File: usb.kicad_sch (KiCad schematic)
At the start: 90 parts, among them J16 USB-C_GCT_USB4105-GF-A, J4 USB-C_GCT_USB4105-GF-A

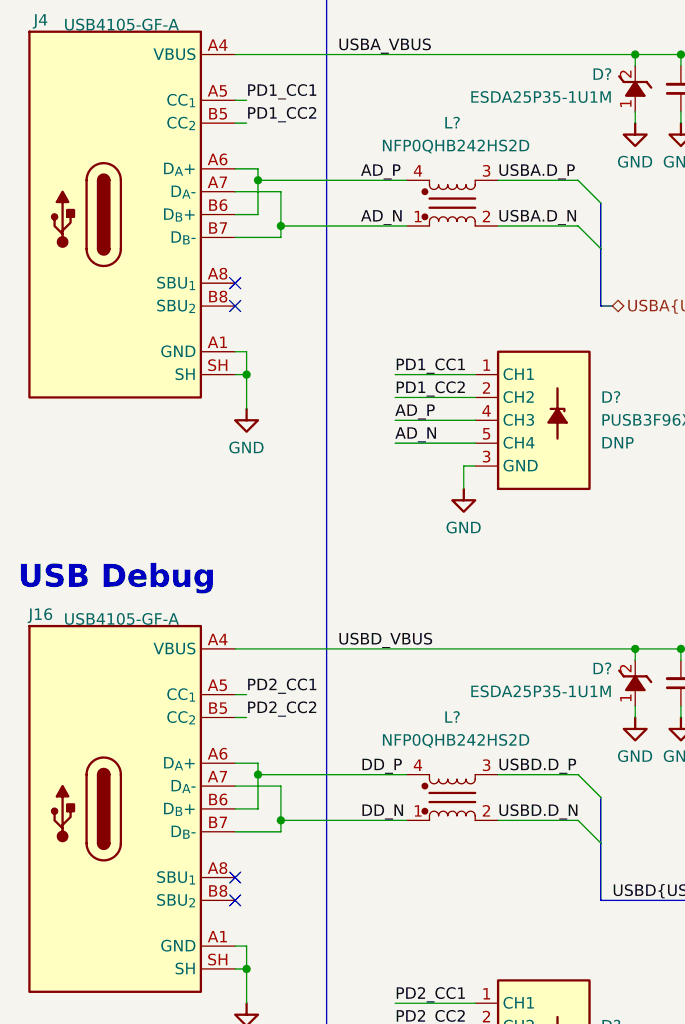
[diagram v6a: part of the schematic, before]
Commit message: [#54617] Migrate to KiCad 7
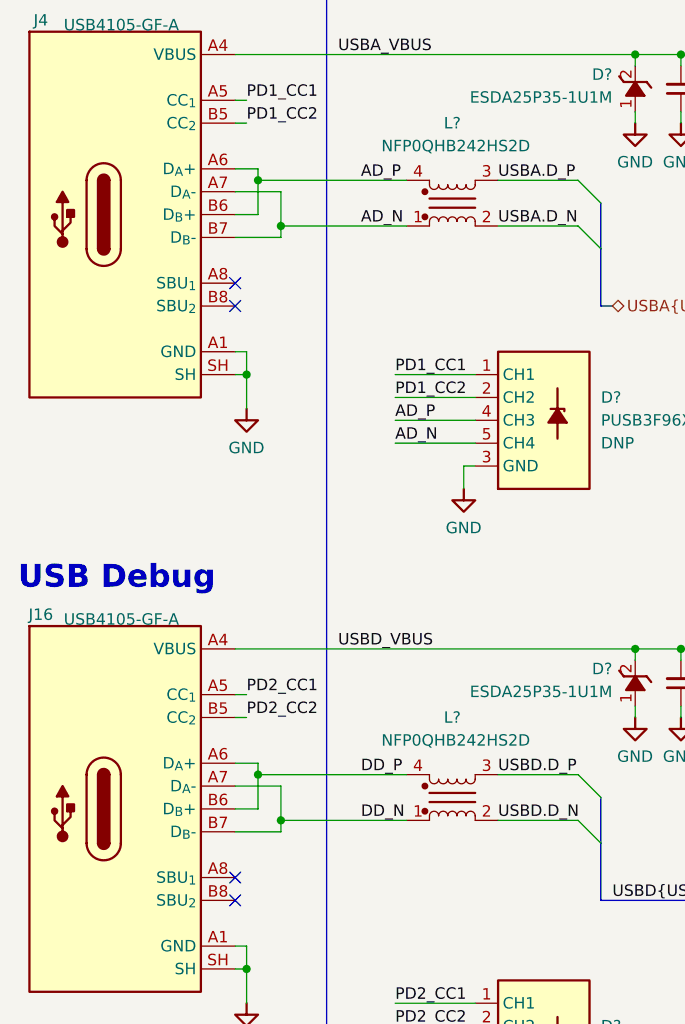
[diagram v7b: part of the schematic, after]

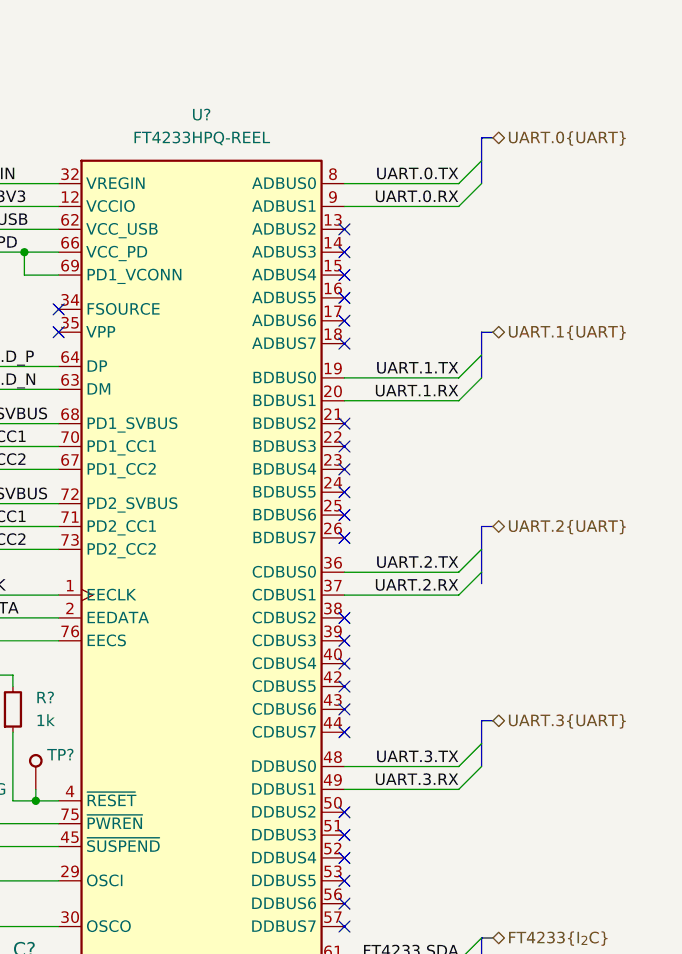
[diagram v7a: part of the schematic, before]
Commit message: [#54617] Fix UART: flip rx/tx
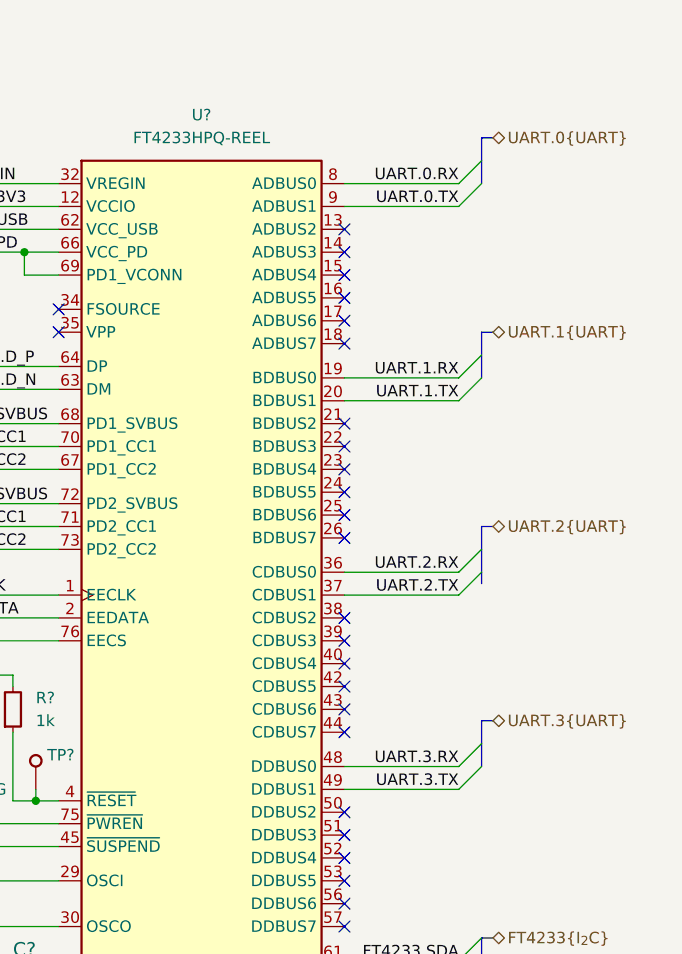
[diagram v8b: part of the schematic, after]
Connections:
- net UART.0.RX: now also U?.8 (ADBUS0); no longer U?.9 (ADBUS1)
- net UART.0.TX: now also U?.9 (ADBUS1); no longer U?.8 (ADBUS0)
- net UART.1.RX: now also U?.19 (BDBUS0); no longer U?.20 (BDBUS1)
- net UART.1.TX: now also U?.20 (BDBUS1); no longer U?.19 (BDBUS0)
- net UART.2.RX: now also U?.36 (CDBUS0); no longer U?.37 (CDBUS1)
- net UART.2.TX: now also U?.37 (CDBUS1); no longer U?.36 (CDBUS0)
- net UART.3.RX: now also U?.48 (DDBUS0); no longer U?.49 (DDBUS1)
- net UART.3.TX: now also U?.49 (DDBUS1); no longer U?.48 (DDBUS0)
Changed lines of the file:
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@@
     (effects (font (size 1.27 1.27)) (justify right bottom))
   )
-  (label "UART.0.TX" (at 381 135.89 180) (fields_autoplaced)
+  (label "UART.0.TX" (at 381 138.43 180) (fields_autoplaced)
     (effects (font (size 1.27 1.27)) (justify right bottom))
   )
@@
     (effects (font (size 1.27 1.27)) (justify right bottom))
   )
-  (label "UART.2.TX" (at 381 179.07 180) (fields_autoplaced)
-    (effects (font (size 1.27 1.27)) (justify right bottom))
-  )
-  (label "UART.1.RX" (at 381 160.02 180) (fields_autoplaced)
+  (label "UART.2.TX" (at 381 181.61 180) (fields_autoplaced)
+    (effects (font (size 1.27 1.27)) (justify right bottom))
+  )
+  (label "UART.1.RX" (at 381 157.48 180) (fields_autoplaced)
     (effects (font (size 1.27 1.27)) (justify right bottom))
   )
@@
     (effects (font (size 1.27 1.27)) (justify left bottom))
   )
-  (label "UART.3.RX" (at 381 203.2 180) (fields_autoplaced)
+  (label "UART.3.RX" (at 381 200.66 180) (fields_autoplaced)
     (effects (font (size 1.27 1.27)) (justify right bottom))
   )
@@
     (effects (font (size 1.27 1.27)) (justify left bottom))
   )
-  (label "UART.2.RX" (at 381 181.61 180) (fields_autoplaced)
+  (label "UART.2.RX" (at 381 179.07 180) (fields_autoplaced)
     (effects (font (size 1.27 1.27)) (justify right bottom))
   )
@@
     (effects (font (size 1.27 1.27)) (justify right bottom))
   )
-  (label "UART.3.TX" (at 381 200.66 180) (fields_autoplaced)
+  (label "UART.3.TX" (at 381 203.2 180) (fields_autoplaced)
     (effects (font (size 1.27 1.27)) (justify right bottom))
   )
@@
     (effects (font (size 1.27 1.27)) (justify left bottom))
   )
-  (label "UART.0.RX" (at 381 138.43 180) (fields_autoplaced)
+  (label "UART.0.RX" (at 381 135.89 180) (fields_autoplaced)
     (effects (font (size 1.27 1.27)) (justify right bottom))
   )
@@
     (effects (font (size 1.27 1.27)) (justify left bottom))
   )
-  (label "UART.1.TX" (at 381 157.48 180) (fields_autoplaced)
-    (effects (font (size 1.27 1.27)) (justify right bottom))
-  )
+  (label "UART.1.TX" (at 381 160.02 180) (fields_autoplaced)
+    (effects (font (size 1.27 1.27)) (justify right bottom))
+  )
